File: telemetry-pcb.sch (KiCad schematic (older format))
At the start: 44 parts, among them CN1 12V_IN, CN10 CAN, CN11 CAN, CN12 CAN_12V_OUT, CN13 THERMO1, CN14 THERMO2, CN15 RS232, CN2 12V_OUT, CN3 12V_OUT, CN4 12V_OUT, CN5 12V_OUT, CN6 CAN, CN7 CAN, CN8 CAN, CN9 CAN, IC1 MAX31855K, IC2 MAX31855K, IC3 TCAN332DR, IC4 MAX3232CPWR, M1 MountingHole, M2 MountingHole, M3 MountingHole, M4 MountingHole, T1 TEST_12V, T2 TEST_3V3, T3 TEST_CAN, T4 GPIO1, T5 GPIO2, T6 TEST_RS232

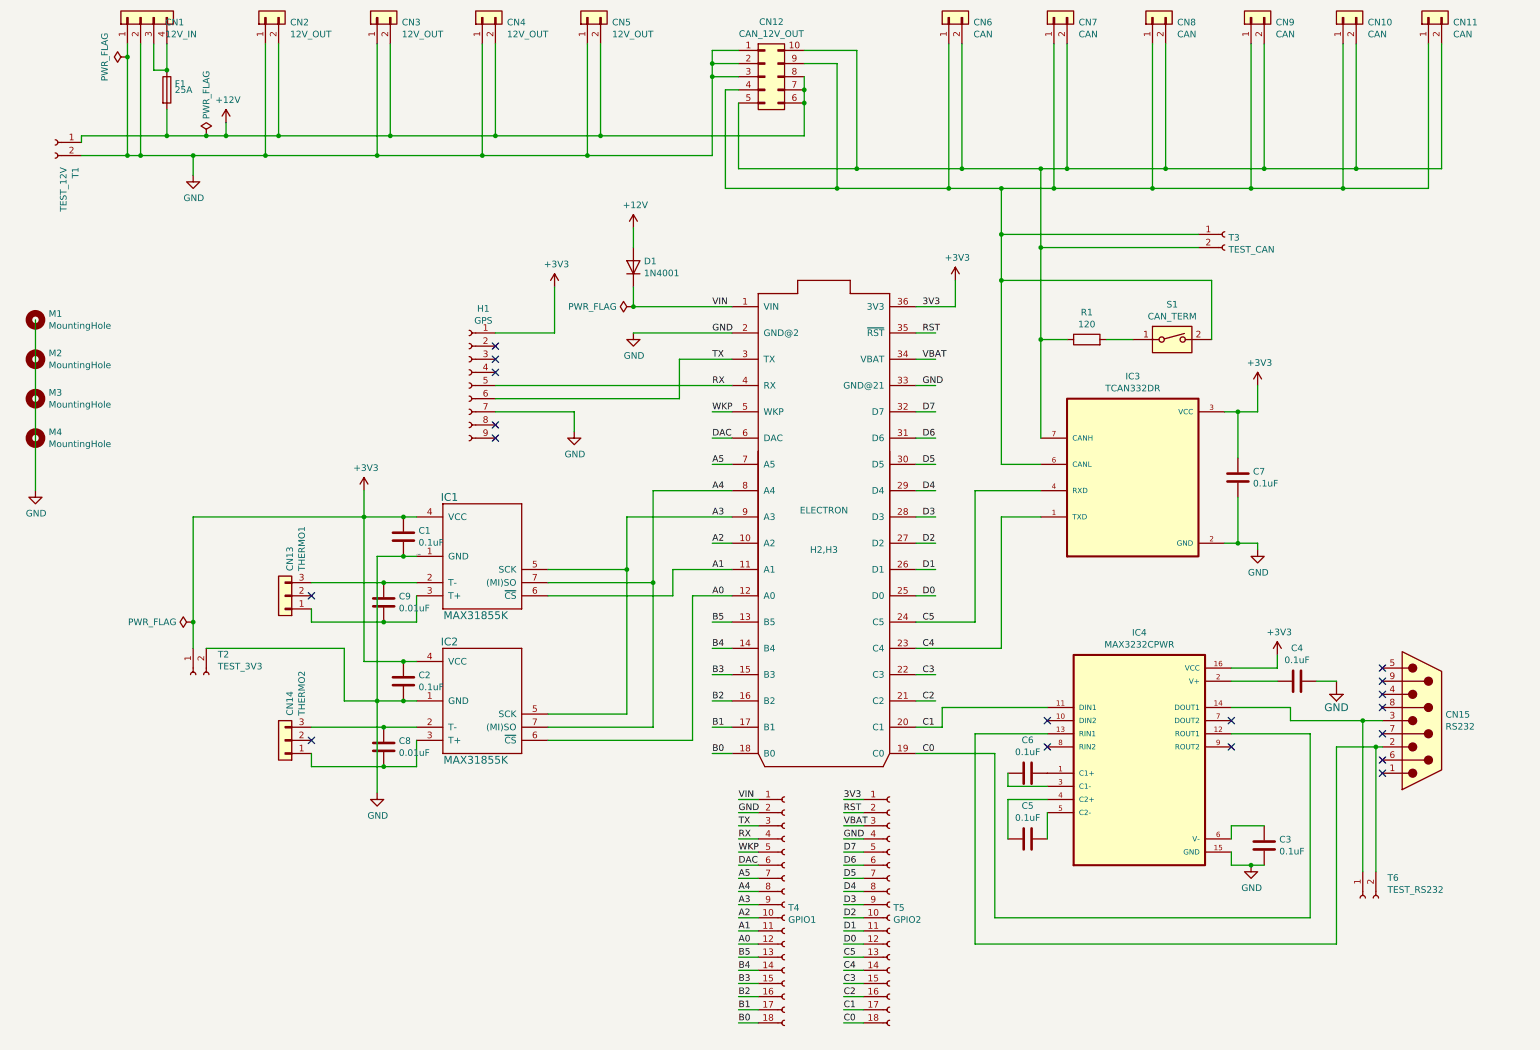
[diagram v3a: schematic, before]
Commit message: finished first draft of schematic with Boron
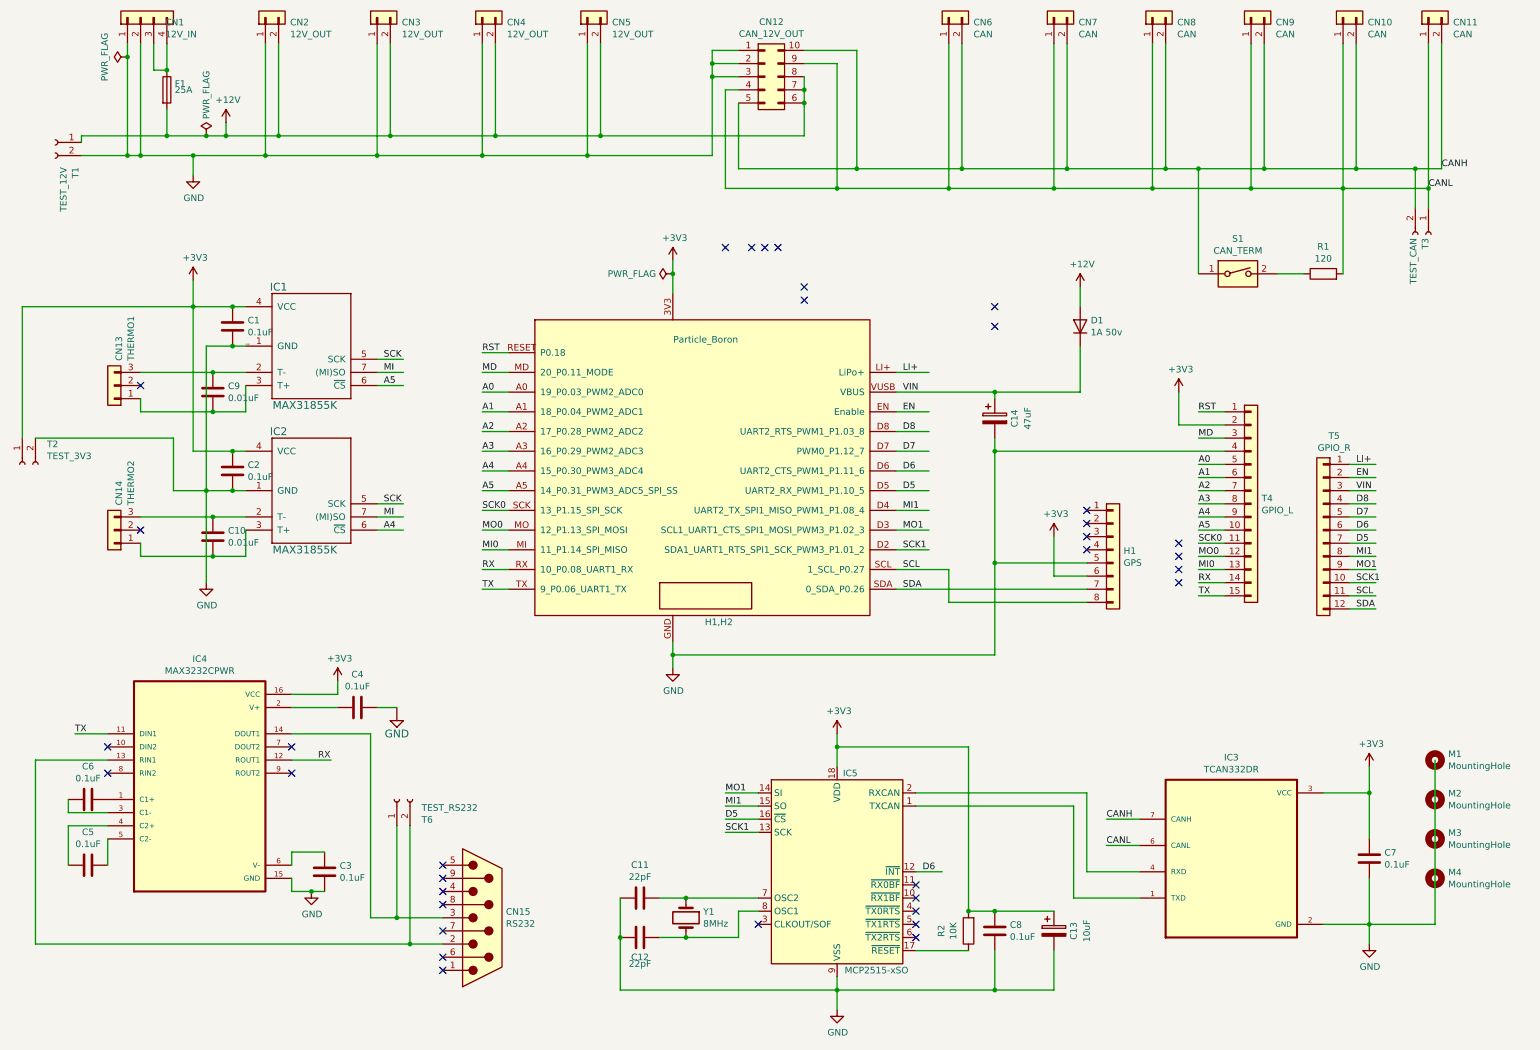
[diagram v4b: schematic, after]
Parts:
- removed H1: GPS, Connector_PinHeader_2.54mm:PinHeader_1x09_P2.54mm_Vertical, symbol Connector:Conn_01x09_Female
- removed H2,H3: ELECTRON, Libraries:electron, symbol telemetry-pcb-eagle-import:ELECTRON_WITH_HEADERS
- removed T4: GPIO1, Connector_PinHeader_2.54mm:PinHeader_1x18_P2.54mm_Vertical, symbol Connector:Conn_01x18_Female
- removed T5: GPIO2, Connector_PinHeader_2.54mm:PinHeader_1x18_P2.54mm_Vertical, symbol Connector:Conn_01x18_Female
- added C11, C12: 22pF, symbol Device:C
- added C13: 10uF, symbol Device:CP
- added C14: 47uF, symbol Device:CP
- added C8: 0.1uF, symbol Device:C
- added H1: GPS, symbol Connector_Generic:Conn_01x08
- added H1,H2: Particle_Boron, symbol particle:Particle_Boron
- added IC5: MCP2515-xSO, Package_SO:SOIC-18W_7.5x11.6mm_P1.27mm, symbol Interface_CAN_LIN:MCP2515-xSO
- added R2: 10K, Resistor_SMD:R_0805_2012Metric, symbol Device:R
- added T4: GPIO_L, symbol Connector_Generic:Conn_01x15
- added T5: GPIO_R, symbol Connector_Generic:Conn_01x12
- added Y1: 8MHz, symbol Device:Crystal
- C7: footprint Capacitor_SMD:C_0805_2012Metric -> (none)
- D1: value 1N4001 -> 1A 50v
- IC3: footprint Package_SO:SOIC-8-1EP_3.9x4.9mm_P1.27mm_EP2.29x3mm -> SOIC127P599X175-8N
- renumbered C8 to C10
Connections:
- net labels added: CANH, CANL, D8, EN, LI+, MD, MI, MI0, MI1, MO0, MO1, SCK, SCK0, SCK1, SCL, SDA
- net labels removed: 3V3, B0, B1, B2, B3, B4, B5, C0, C1, C2, C3, C4, C5, D0, D1, D2, D3, D4, DAC, VBAT, WKP
- wire segments 259 -> 257
- no-connect marks 18 -> 35
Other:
- moved on the sheet: C1, C10, C2, C3, C4, C5, C6, C9, CN13, CN14, CN15, D1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

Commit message: finished first draft of schematic for Boron
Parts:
- added C15: 0.1uF, Capacitor_SMD:C_0805_2012Metric, symbol Device:C
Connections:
- wire segments 257 -> 260
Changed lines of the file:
@@
 	2350 6850 2350 6950
-Wire Wire Line
-	2700 5450 2700 5350
 Wire Wire Line
 	2350 5450 2700 5450
@@
 L power:+3V3 #PWR0114
 U 1 1 60559060
-P 2700 5350
-F 0 "#PWR0114" H 2700 5200 50  0001 C CNN
-F 1 "+3V3" H 2715 5523 50  0000 C CNN
-F 2 "" H 2700 5350 50  0001 C CNN
-F 3 "" H 2700 5350 50  0001 C CNN
-	1    2700 5350
+P 2700 4850
+F 0 "#PWR0114" H 2700 4700 50  0001 C CNN
+F 1 "+3V3" H 2715 5023 50  0000 C CNN
+F 2 "" H 2700 4850 50  0001 C CNN
+F 3 "" H 2700 4850 50  0001 C CNN
+	1    2700 4850
 	1    0    0    -1
 $EndComp
@@
 Wire Wire Line
 	6950 3600 7200 3600
-Wire Wire Line
-	6950 3750 7200 3750
 Wire Wire Line
 	6950 3900 7200 3900
@@
 NoConn ~ 8400 4250
 NoConn ~ 8400 4350
+Wire Wire Line
+	3150 5150 3150 5550
+Connection ~ 3150 5550
+Wire Wire Line
+	2700 4850 2700 5150
+Wire Wire Line
+	2700 5150 2700 5450
+Connection ~ 2700 5150
+Wire Wire Line
+	3000 5150 3150 5150
+$Comp
+L Device:C C15
+U 1 1 602F2388
+P 2850 5150
+F 0 "C15" V 2598 5150 50  0000 C CNN
+F 1 "0.1uF" V 2689 5150 50  0000 C CNN
+F 2 "Capacitor_SMD:C_0805_2012Metric" H 2888 5000 50  0001 C CNN
+F 3 "~" H 2850 5150 50  0001 C CNN
+	1    2850 5150
+	0    1    1    0
+$EndComp
+Wire Wire Line
+	6950 3750 7200 3750
 $EndSCHEMATC

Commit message: finished footprint selection, placement, and silkscreen.
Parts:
- C11, C12, C7, C8: footprint (none) -> Capacitor_SMD:C_0805_2012Metric
- C13: footprint (none) -> Capacitor_SMD:C_1206_3216Metric
- C14: footprint (none) -> Capacitor_SMD:CP_Elec_6.3x5.4
- CN13, CN14: footprint Conn_Molex_70553-0002:Molex-70553-0002-0-0-0 -> Conn_Molex_70553-0002:Molex-70551-0002-0-0-0
- CN15: footprint Connector_Dsub:DSUB-9_Male_Horizontal_P2.77x2.54mm_EdgePinOffset9.40mm -> Libraries:DLS1XP5AK40X
- CN2, CN3, CN4, CN5: footprint Connector_Molex:Molex_Mega-Fit_76825-0002_2x01_P5.70mm_Horizontal -> Connector_Molex:Molex_Mega-Fit_76825-0004_1x02_P5.70mm_Horizontal
- H1,H2: footprint (none) -> Libraries:PCB_FeatherWing
- H3,H4: renamed from H1; footprint (none) -> Connector_PinSocket_2.54mm:PinSocket_1x08_P2.54mm_Vertical
- IC3: footprint SOIC127P599X175-8N -> Libraries:SOIC127P599X175-8N
- T4: footprint (none) -> Connector_PinSocket_2.54mm:PinSocket_1x15_P2.54mm_Vertical
- T5: footprint (none) -> Connector_PinSocket_2.54mm:PinSocket_1x12_P2.54mm_Vertical
- Y1: footprint (none) -> Crystal:Crystal_SMD_HC49-SD
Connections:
- no-connect marks 35 -> 27
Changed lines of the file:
@@
 F 0 "CN3" V 2964 112 50  0000 R CNN
 F 1 "12V_OUT" V 2873 112 50  0000 R CNN
-F 2 "Connector_Molex:Molex_Mega-Fit_76825-0002_2x01_P5.70mm_Horizontal" H 3000 300 50  0001 C CNN
+F 2 "Connector_Molex:Molex_Mega-Fit_76825-0004_1x02_P5.70mm_Horizontal" H 3000 300 50  0001 C CNN
 F 3 "~" H 3000 300 50  0001 C CNN
 	1    3000 300
@@
 F 0 "CN2" V 2114 112 50  0000 R CNN
 F 1 "12V_OUT" V 2023 112 50  0000 R CNN
-F 2 "Connector_Molex:Molex_Mega-Fit_76825-0002_2x01_P5.70mm_Horizontal" H 2150 300 50  0001 C CNN
+F 2 "Connector_Molex:Molex_Mega-Fit_76825-0004_1x02_P5.70mm_Horizontal" H 2150 300 50  0001 C CNN
 F 3 "~" H 2150 300 50  0001 C CNN
 	1    2150 300
@@
 F 0 "CN4" V 3764 112 50  0000 R CNN
 F 1 "12V_OUT" V 3673 112 50  0000 R CNN
-F 2 "Connector_Molex:Molex_Mega-Fit_76825-0002_2x01_P5.70mm_Horizontal" H 3800 300 50  0001 C CNN
+F 2 "Connector_Molex:Molex_Mega-Fit_76825-0004_1x02_P5.70mm_Horizontal" H 3800 300 50  0001 C CNN
 F 3 "~" H 3800 300 50  0001 C CNN
 	1    3800 300
@@
 F 0 "CN5" V 4564 112 50  0000 R CNN
 F 1 "12V_OUT" V 4473 112 50  0000 R CNN
-F 2 "Connector_Molex:Molex_Mega-Fit_76825-0002_2x01_P5.70mm_Horizontal" H 4600 300 50  0001 C CNN
+F 2 "Connector_Molex:Molex_Mega-Fit_76825-0004_1x02_P5.70mm_Horizontal" H 4600 300 50  0001 C CNN
 F 3 "~" H 4600 300 50  0001 C CNN
 	1    4600 300
@@
 F 0 "CN14" V 964 4012 50  0000 R CNN
 F 1 "THERMO2" V 873 4012 50  0000 R CNN
-F 2 "Conn_Molex_70553-0002:Molex-70553-0002-0-0-0" H 1000 4200 50  0001 C CNN
+F 2 "Conn_Molex_70553-0002:Molex-70551-0002-0-0-0" H 1000 4200 50  0001 C CNN
 F 3 "~" H 1000 4200 50  0001 C CNN
 	1    1000 4200
@@
 F 0 "CN13" V 964 2912 50  0000 R CNN
 F 1 "THERMO1" V 873 2912 50  0000 R CNN
-F 2 "Conn_Molex_70553-0002:Molex-70553-0002-0-0-0" H 1000 3100 50  0001 C CNN
+F 2 "Conn_Molex_70553-0002:Molex-70551-0002-0-0-0" H 1000 3100 50  0001 C CNN
 F 3 "~" H 1000 3100 50  0001 C CNN
 	1    1000 3100
@@
 Wire Wire Line
 	7450 1450 8250 1450
-NoConn ~ 5650 2050
-NoConn ~ 5850 2050
-NoConn ~ 5950 2050
-NoConn ~ 6050 2050
-NoConn ~ 6250 2350
-NoConn ~ 6250 2450
-NoConn ~ 7700 2500
-NoConn ~ 7700 2650
 Wire Wire Line
 	5250 5050 5250 5150
@@
 F 0 "CN15" H 3980 7196 50  0000 L CNN
 F 1 "RS232" H 3980 7105 50  0000 L CNN
-F 2 "Connector_Dsub:DSUB-9_Male_Horizontal_P2.77x2.54mm_EdgePinOffset9.40mm" H 3800 7150 50  0001 C CNN
+F 2 "Libraries:DLS1XP5AK40X" H 3800 7150 50  0001 C CNN
 F 3 " ~" H 3800 7150 50  0001 C CNN
 	1    3800 7150
@@
 F 0 "Y1" V 5304 7281 50  0000 L CNN
 F 1 "8MHz" V 5395 7281 50  0000 L CNN
-F 2 "" H 5350 7150 50  0001 C CNN
+F 2 "Crystal:Crystal_SMD_HC49-SD" H 5350 7150 50  0001 C CNN
 F 3 "~" H 5350 7150 50  0001 C CNN
 	1    5350 7150
@@
 F 0 "C11" V 4748 7000 50  0000 C CNN
 F 1 "22pF" V 4839 7000 50  0000 C CNN
-F 2 "" H 5038 6850 50  0001 C CNN
+F 2 "Capacitor_SMD:C_0805_2012Metric" H 5038 6850 50  0001 C CNN
 F 3 "~" H 5000 7000 50  0001 C CNN
 	1    5000 7000
@@
 F 0 "C12" V 5150 7300 50  0000 C CNN
 F 1 "22pF" V 5200 7300 50  0000 C CNN
-F 2 "" H 5038 7150 50  0001 C CNN
+F 2 "Capacitor_SMD:C_0805_2012Metric" H 5038 7150 50  0001 C CNN
 F 3 "~" H 5000 7300 50  0001 C CNN
 	1    5000 7300
@@
 F 0 "C8" H 7585 7204 50  0000 R CNN
 F 1 "0.1uF" H 7585 7295 50  0000 R CNN
-F 2 "" H 7738 7100 50  0001 C CNN
+F 2 "Capacitor_SMD:C_0805_2012Metric" H 7738 7100 50  0001 C CNN
 F 3 "~" H 7700 7250 50  0001 C CNN
 	1    7700 7250
@@
 F 0 "C13" V 8300 7250 50  0000 C CNN
 F 1 "10uF" V 8400 7250 50  0000 C CNN
-F 2 "" H 8188 7100 50  0001 C CNN
+F 2 "Capacitor_SMD:C_1206_3216Metric" H 8188 7100 50  0001 C CNN
 F 3 "~" H 8150 7250 50  0001 C CNN
 	1    8150 7250
@@
 F 0 "IC3" H 9500 7470 50  0000 C CNN
 F 1 "TCAN332DR" H 9500 7379 50  0000 C CNN
-F 2 "SOIC127P599X175-8N" H 9500 6700 50  0001 L BNN
+F 2 "Libraries:SOIC127P599X175-8N" H 9500 6700 50  0001 L BNN
 F 3 "" H 9500 6700 50  0001 L BNN
 	1    9500 6700
@@
 F 0 "C7" H 10435 6654 50  0000 R CNN
 F 1 "0.1uF" H 10435 6745 50  0000 R CNN
-F 2 "" H 10588 6550 50  0001 C CNN
+F 2 "Capacitor_SMD:C_0805_2012Metric" H 10588 6550 50  0001 C CNN
 F 3 "~" H 10550 6700 50  0001 C CNN
 	1    10550 6700
@@
 F 0 "C14" V 7850 3350 50  0000 C CNN
 F 1 "47uF" V 7950 3350 50  0000 C CNN
-F 2 "" H 7738 3200 50  0001 C CNN
+F 2 "Capacitor_SMD:CP_Elec_6.3x5.4" H 7738 3200 50  0001 C CNN
 F 3 "~" H 7700 3350 50  0001 C CNN
 	1    7700 3350
 	1    0    0    -1
 $EndComp
-$Comp
-L particle:Particle_Boron H1,H2
-U 1 1 602A0E66
-P 5450 3600
-F 0 "H1,H2" H 5600 2300 50  0000 C CNN
-F 1 "Particle_Boron" H 5500 4450 50  0000 C CNN
-F 2 "" H 4750 3800 50  0001 C CNN
-F 3 "" H 4750 3800 50  0001 C CNN
-	1    5450 3600
-	1    0    0    -1
-$EndComp
 Wire Wire Line
 	6950 3150 7700 3150
 $Comp
-L Connector_Generic:Conn_01x08 H1
+L Connector_Generic:Conn_01x08 H3,H4
 U 1 1 602E3E90
 P 8600 4350
-F 0 "H1" H 8680 4342 50  0000 L CNN
+F 0 "H3,H4" H 8680 4342 50  0000 L CNN
 F 1 "GPS" H 8680 4251 50  0000 L CNN
-F 2 "" H 8600 4350 50  0001 C CNN
+F 2 "Connector_PinSocket_2.54mm:PinSocket_1x08_P2.54mm_Vertical" H 8600 4350 50  0001 C CNN
 F 3 "~" H 8600 4350 50  0001 C CNN
 	1    8600 4350
@@
 F 0 "T4" H 9730 4042 50  0000 L CNN
 F 1 "GPIO_L" H 9730 3951 50  0000 L CNN
-F 2 "" H 9650 4000 50  0001 C CNN
+F 2 "Connector_PinSocket_2.54mm:PinSocket_1x15_P2.54mm_Vertical" H 9650 4000 50  0001 C CNN
 F 3 "~" H 9650 4000 50  0001 C CNN
 	1    9650 4000
@@
 F 0 "T5" H 10118 4917 50  0000 C CNN
 F 1 "GPIO_R" H 10118 4826 50  0000 C CNN
-F 2 "" H 10200 4200 50  0001 C CNN
+F 2 "Connector_PinSocket_2.54mm:PinSocket_1x12_P2.54mm_Vertical" H 10200 4200 50  0001 C CNN
 F 3 "~" H 10200 4200 50  0001 C CNN
 	1    10200 4200
@@
 Wire Wire Line
 	6950 3750 7200 3750
+$Comp
+L particle:Particle_Boron H1,H2
+U 1 1 602A0E66
+P 5450 3600
+F 0 "H1,H2" H 5600 2300 50  0000 C CNN
+F 1 "Particle_Boron" H 5500 4450 50  0000 C CNN
+F 2 "Libraries:PCB_FeatherWing" H 4750 3800 50  0001 C CNN
+F 3 "" H 4750 3800 50  0001 C CNN
+	1    5450 3600
+	1    0    0    -1
+$EndComp
 $EndSCHEMATC

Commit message: updated PCB to fix two errors: TX/RX were switched on DB9 jack, and SPI was not connected to MAX31855 ICs
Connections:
- net labels added: MO
- net labels removed: MI0, MO0, SCK0
- wire segments 260 -> 261
- no-connect marks 27 -> 23
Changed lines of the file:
@@
 $EndComp
 Wire Wire Line
-	400  5950 400  7350
-Wire Wire Line
-	2950 5750 2950 7150
-Wire Wire Line
-	2350 5750 2950 5750
-Wire Wire Line
-	2950 7150 3150 7150
-Wire Wire Line
-	3150 7150 3150 6450
-Connection ~ 3150 7150
-Wire Wire Line
-	3150 7150 3500 7150
-Wire Wire Line
-	400  7350 3250 7350
-Wire Wire Line
-	3250 6450 3250 7350
-Connection ~ 3250 7350
-Wire Wire Line
-	3250 7350 3500 7350
+	400  5950 400  7150
 Wire Wire Line
 	2350 5950 2650 5950
@@
 TX
 Text Label 3800 4350 0    50   ~ 0
-MI0
+MI
 Text Label 3800 4200 0    50   ~ 0
-MO0
+MO
 Text Label 3800 4050 0    50   ~ 0
-SCK0
+SCK
 Wire Wire Line
 	3000 2900 3200 2900
@@
 	1    0    0    -1
 $EndComp
-NoConn ~ 9100 4300
-NoConn ~ 9100 4400
-NoConn ~ 9100 4500
-NoConn ~ 9100 4600
 Wire Wire Line
 	6950 4500 7350 4500
@@
 A5
 Text Label 9250 4300 0    50   ~ 0
-SCK0
+SCK
 Text Label 9250 4400 0    50   ~ 0
-MO0
+MO
 Text Label 9250 4500 0    50   ~ 0
-MI0
+MI
 Text Label 9250 4600 0    50   ~ 0
 RX
@@
 	1    0    0    -1
 $EndComp
+Wire Wire Line
+	400  7150 3250 7150
+Wire Wire Line
+	3250 7150 3250 6450
+Connection ~ 3250 7150
+Wire Wire Line
+	3250 7150 3500 7150
+Wire Wire Line
+	3150 7350 3150 6600
+Wire Wire Line
+	3150 7350 3500 7350
+Wire Wire Line
+	3150 6600 2800 6600
+Wire Wire Line
+	2800 6600 2800 5750
+Wire Wire Line
+	2800 5750 2350 5750
+Connection ~ 3150 6600
+Wire Wire Line
+	3150 6600 3150 6450
 $EndSCHEMATC

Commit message: made some final changes to PCB and BOM
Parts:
- renumbered H3,H4 to H3
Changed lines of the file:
@@
 	6950 3150 7700 3150
 $Comp
-L Connector_Generic:Conn_01x08 H3,H4
+L Connector_Generic:Conn_01x08 H3
 U 1 1 602E3E90
 P 8600 4350
-F 0 "H3,H4" H 8680 4342 50  0000 L CNN
+F 0 "H3" H 8680 4342 50  0000 L CNN
 F 1 "GPS" H 8680 4251 50  0000 L CNN
 F 2 "Connector_PinSocket_2.54mm:PinSocket_1x08_P2.54mm_Vertical" H 8600 4350 50  0001 C CNN
